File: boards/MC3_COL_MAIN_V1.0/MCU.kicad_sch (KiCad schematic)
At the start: 47 parts, among them J2 SWD, SW1 SKRKAEE020, U10 GP1S094HCZ0F, U11 GP1S094HCZ0F, U2 STM32U595RJT6, U9 AEDR-8300-1Q0, Y1 8MHz

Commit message: WIP checkpoint before LED chain (board session state as on disk)
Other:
- moved on the sheet: R6, R7

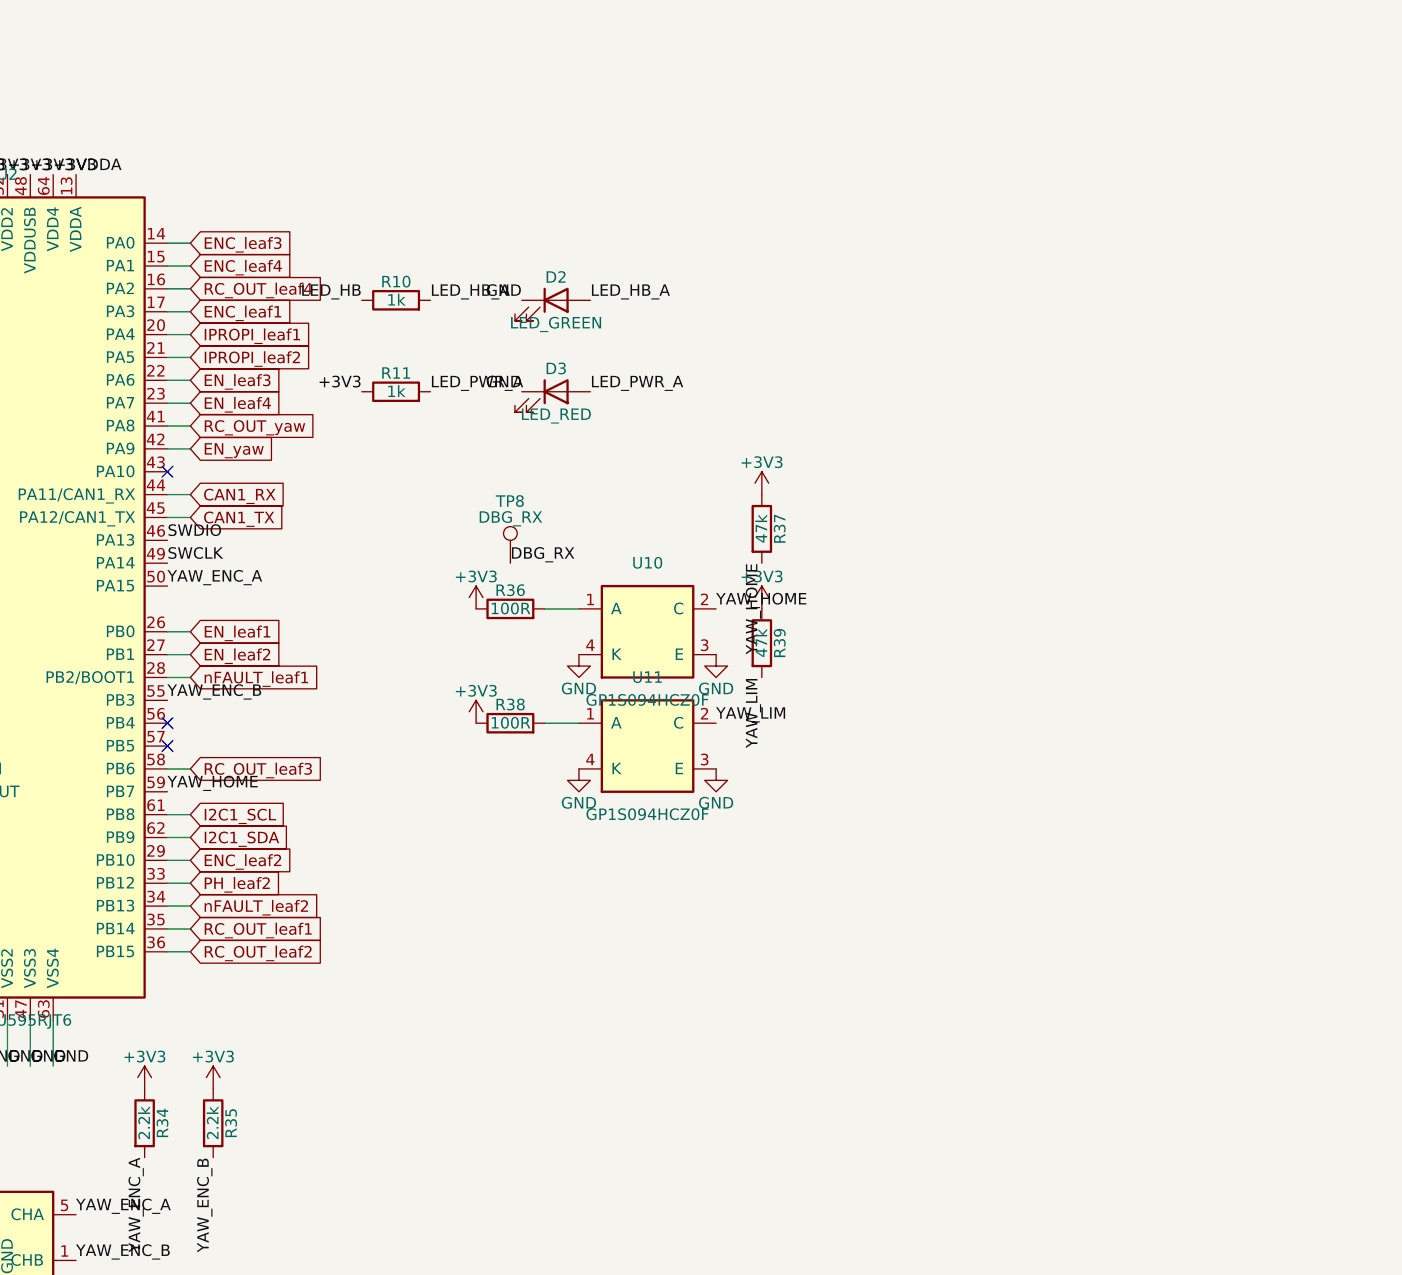
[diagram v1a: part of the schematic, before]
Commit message: Status pixels: 4x XL-1010RGBC-WS2812B chain D5-D8 on VM, R40 470R, C44-C47; LED_DATA on PB5/SPI1_MOSI; symbol + LED_XL-1010RGBC footprint; MIGRATION s13 (COL-COTS-0036)
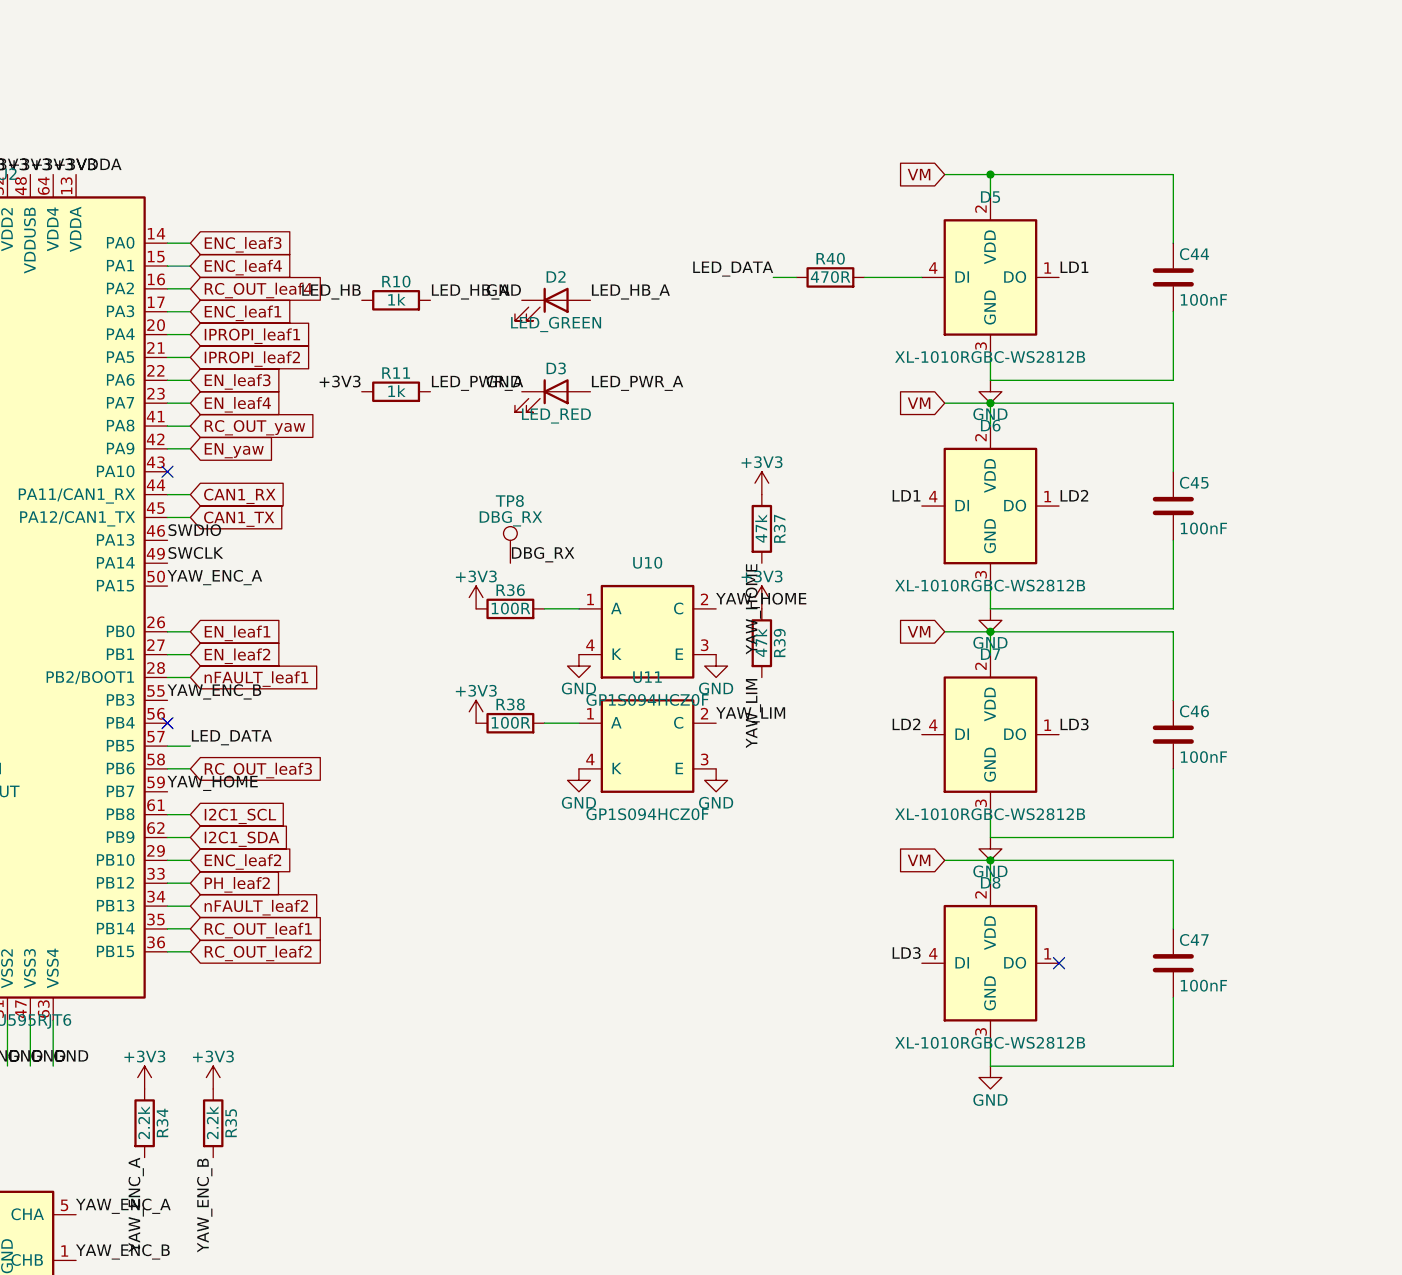
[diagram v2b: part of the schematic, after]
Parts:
- added C44, C45, C46, C47: 100nF, MC3_COL_MAIN:C_0402_1005Metric, symbol Device:C
- added D5, D6, D7, D8: XL-1010RGBC-WS2812B, MC3_COL_MAIN:LED_XL-1010RGBC, symbol MC3_COL_MAIN:XL-1010RGBC-WS2812B
- added R40: 470R, MC3_COL_MAIN:R_0402_1005Metric, symbol Device:R
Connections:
- net GND: now also C44.2, C45.2, C46.2, C47.2, D5.3 (GND), D6.3 (GND), D7.3 (GND), D8.3 (GND)
- net LED_DATA: now reaches U2.57 (PB5)
- net LED_DATA: now also R40.1
- new net: D5.4 (DI), R40.2
- new net LD1: D5.1 (DO), D6.4 (DI)
- new net LD2: D6.1 (DO), D7.4 (DI)
- new net LD3: D7.1 (DO), D8.4 (DI)
- new net VM: C44.1, C45.1, C46.1, C47.1, D5.2 (VDD), D6.2 (VDD), D7.2 (VDD), D8.2 (VDD)

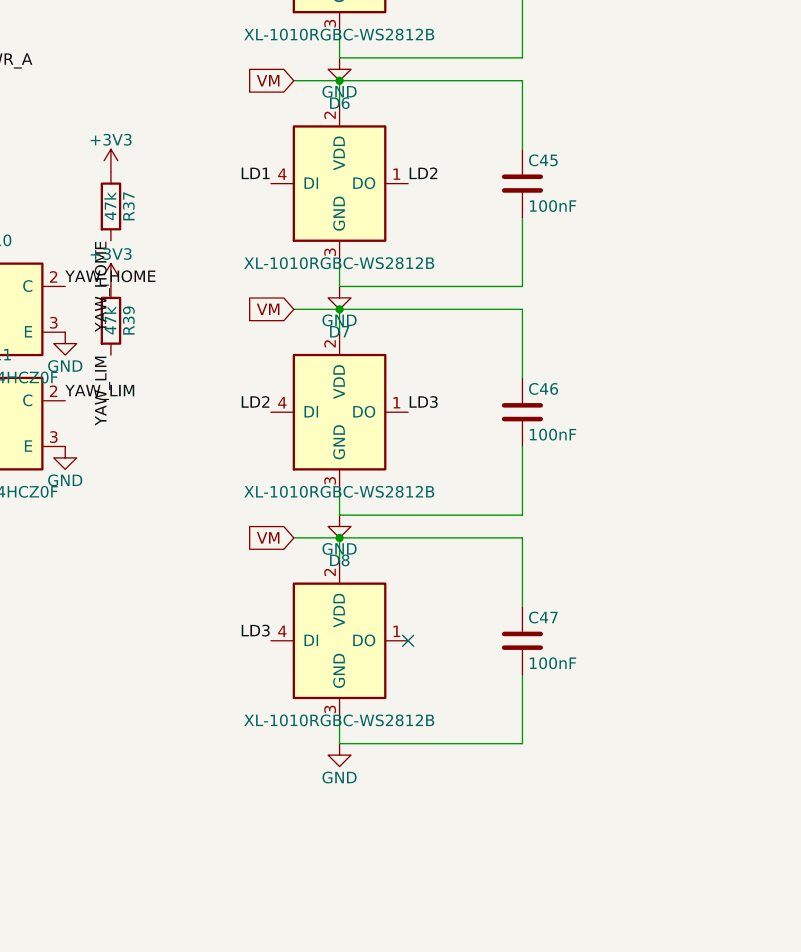
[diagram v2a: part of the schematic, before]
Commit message: Status pixels cut to two (D5-D6, C44-C45); D7/D8/C46/C47 removed, D6 DO no-connect
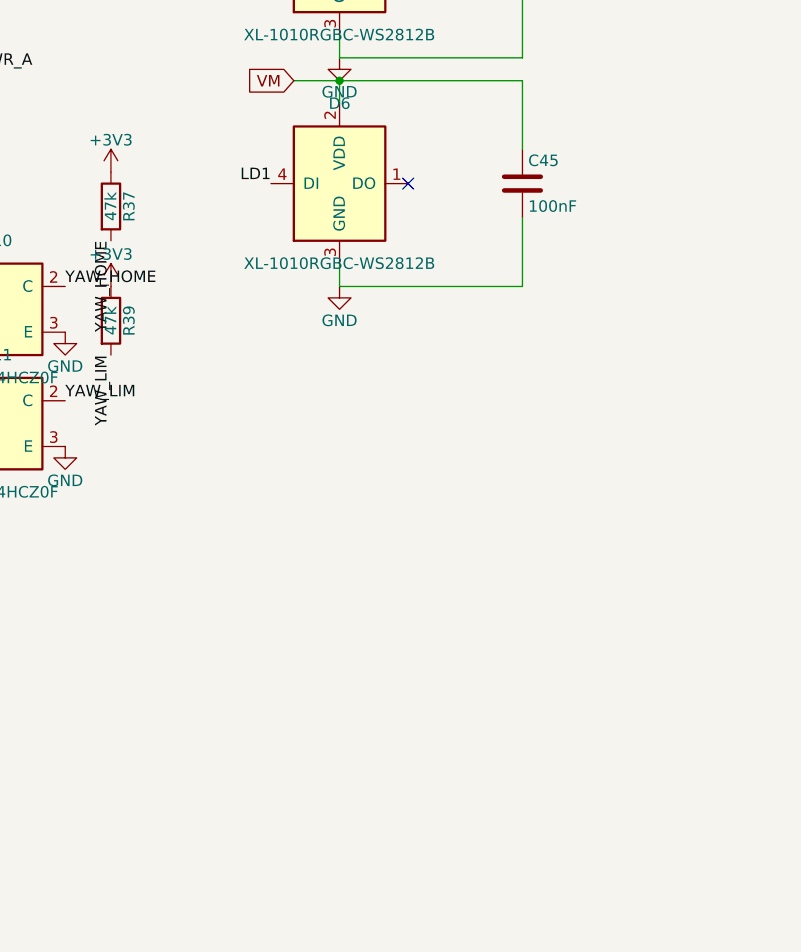
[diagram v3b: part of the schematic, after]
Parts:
- removed C46, C47: 100nF, MC3_COL_MAIN:C_0402_1005Metric, symbol Device:C
- removed D7, D8: XL-1010RGBC-WS2812B, MC3_COL_MAIN:LED_XL-1010RGBC, symbol MC3_COL_MAIN:XL-1010RGBC-WS2812B
- D5: Note PROVISIONAL - addressable RGB status pixel 1 of 4, chain he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 -> PROVISIONAL - addressable RGB status pixel 1 of 2, chain he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
- D6: Note PROVISIONAL - status pixel 2 of 4. See D5. -> PROVISIONAL - status pixel 2 of 2, chain tail (DO no-connec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
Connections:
- net LD2: no longer names the net of D6.1 (DO)
